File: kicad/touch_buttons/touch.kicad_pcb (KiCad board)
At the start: 2 copper layers, 15.7 x 15.7 mm, 3 parts, among them J1 CONN_01X03

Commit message: update
- drawing buttons
- still to finish
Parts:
- removed 2M1: R, Touch_conn:res
- removed J1: CONN_01X03, Touch_conn:touch_conn
- removed JP1: touch, Touch_conn:touch
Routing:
- net Net-(2M1-Pad2): track 36.9 -> 0.00 mm, vias 1 -> 0
- net Net-(2M1-Pad1): track 12.2 -> 0.00 mm
- net (no net): track 0.51 -> 0.00 mm, vias 1 -> 0
- removed copper zone on B.Cu, net GND
- removed copper zone on F.Cu, net GND
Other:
- board size 15.7 x 15.7 mm -> 15 x 15 mm

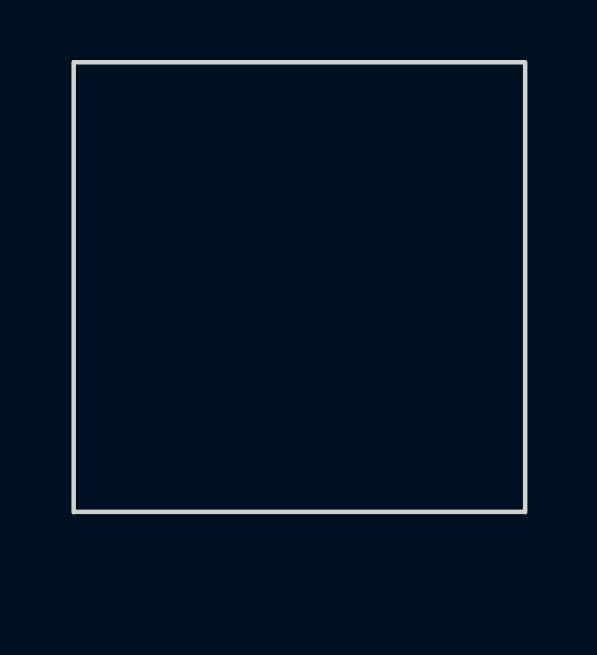
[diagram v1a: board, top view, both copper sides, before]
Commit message: update
- try to make a better button
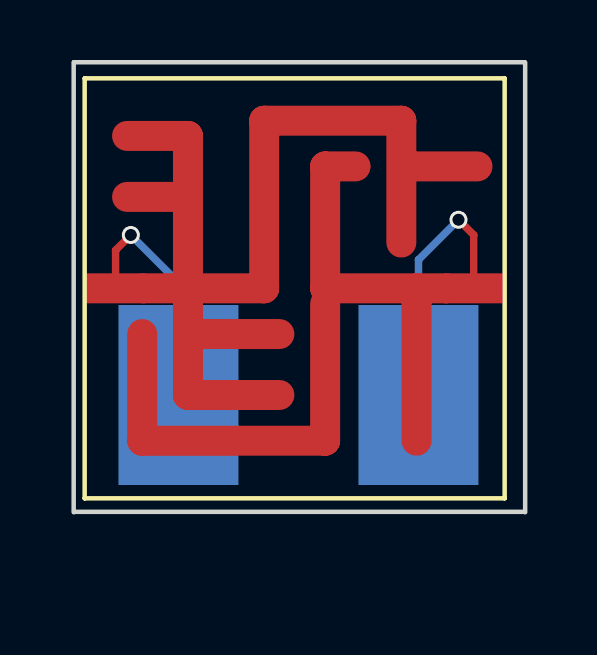
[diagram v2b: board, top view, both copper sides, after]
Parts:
- added J1: CONN_01X02, touch_conn, B.Cu at (157.5, 101.1)
- added JP1: touch, touch_zig, F.Cu at (157.4, 97.5)
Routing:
- net Net-(J1-Pad1): track 0.00 -> 8.89 mm, vias 0 -> 1
- net GND: track 0.00 -> 7.98 mm, vias 0 -> 1
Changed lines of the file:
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@@
-(kicad_pcb (version 4) (host pcbnew 4.0.6)
+(kicad_pcb (version 4) (host pcbnew 4.0.7)
   (general
-    (links 0)
+    (links 2)
     (no_connects 0)
-    (area 149.530999 91.110999 165.429001 107.009001)
+    (area 149.911999 89.924999 165.111501 105.075001)
     (thickness 1.6)
     (drawings 6)
-    (tracks 0)
+    (tracks 10)
     (zones 0)
-    (modules 0)
-    (nets 1)
+    (modules 2)
+    (nets 3)
   )
   (page A4)
@@
     (pad_drill 0)
     (pad_to_mask_clearance 0.2)
-    (aux_axis_origin 0 0)
+    (aux_axis_origin 188.468 96.3295)
     (visible_elements 7FFFFFFF)
     (pcbplotparams
@@
   )
   (net 0 "")
+  (net 1 "Net-(J1-Pad1)")
+  (net 2 GND)
   (net_class Default "This is the default net class."
     (clearance 0.2)
@@
     (uvia_dia 0.3)
     (uvia_drill 0.1)
+    (add_net GND)
+    (add_net "Net-(J1-Pad1)")
+  )
+  (module touch_zig (layer F.Cu)
+    (at 157.353 97.536)
+    (fp_text reference JP1 (at 0 9.652) (layer F.Fab)
+      (effects (font (size 1 1) (thickness 0.15)))
+    )
+    (fp_text value touch (at 0 8.128) (layer F.Fab)
+      (effects (font (size 1 1) (thickness 0.15)))
+    )
+    (fp_line (start 5.08 0) (end 1.016 0) (layer F.Cu) (width 1))
+    (fp_line (start -5.08 0) (end -1.016 0) (layer F.Cu) (width 1))
+    (fp_line (start 3.556 -5.588) (end 3.556 -1.524) (layer F.Cu) (width 1))
+    (fp_line (start -1.016 -5.588) (end 3.556 -5.588) (layer F.Cu) (width 1))
+    (fp_line (start -1.016 0) (end -1.016 -5.588) (layer F.Cu) (width 1))
+    (fp_line (start 1.016 -4.064) (end 2.032 -4.064) (layer F.Cu) (width 1))
+    (fp_line (start 1.016 0) (end 1.016 -4.064) (layer F.Cu) (width 1))
+    (fp_line (start -5.08 5.08) (end -5.08 1.524) (layer F.Cu) (width 1))
+    (fp_line (start 1.016 5.08) (end -5.08 5.08) (layer F.Cu) (width 1))
+    (fp_line (start 1.016 0.508) (end 1.016 5.08) (layer F.Cu) (width 1))
+    (fp_line (start -3.556 3.556) (end -0.508 3.556) (layer F.Cu) (width 1))
+    (fp_line (start -3.556 0.508) (end -3.556 3.556) (layer F.Cu) (width 1))
+    (fp_line (start -3.556 -5.08) (end -5.588 -5.08) (layer F.Cu) (width 1))
+    (fp_line (start -3.556 -0.508) (end -3.556 -5.08) (layer F.Cu) (width 1))
+    (fp_line (start 4.064 0) (end 4.064 5.08) (layer F.Cu) (width 1))
+    (fp_line (start 4.064 -4.064) (end 6.096 -4.064) (layer F.Cu) (width 1))
+    (fp_line (start -4.064 -3.048) (end -5.588 -3.048) (layer F.Cu) (width 1))
+    (fp_line (start -3.048 1.524) (end -0.508 1.524) (layer F.Cu) (width 1))
+    (fp_line (start -3.048 1.524) (end -0.508 1.524) (layer F.Mask) (width 1))
+    (fp_line (start -4.064 -3.048) (end -5.588 -3.048) (layer F.Mask) (width 1))
+    (fp_line (start 4.064 -4.064) (end 6.096 -4.064) (layer F.Mask) (width 1))
+    (fp_line (start 4.064 0) (end 4.064 5.08) (layer F.Mask) (width 1))
+    (fp_line (start -3.556 -0.508) (end -3.556 -5.08) (layer F.Mask) (width 1))
+    (fp_line (start -3.556 -5.08) (end -5.588 -5.08) (layer F.Mask) (width 1))
+    (fp_line (start -3.556 0.508) (end -3.556 3.556) (layer F.Mask) (width 1))
+    (fp_line (start -3.556 3.556) (end -0.508 3.556) (layer F.Mask) (width 1))
+    (fp_line (start 1.016 0.508) (end 1.016 5.08) (layer F.Mask) (width 1))
+    (fp_line (start 1.016 5.08) (end -5.08 5.08) (layer F.Mask) (width 1))
+    (fp_line (start -5.08 5.08) (end -5.08 1.524) (layer F.Mask) (width 1))
+    (fp_line (start 1.016 0) (end 1.016 -4.064) (layer F.Mask) (width 1))
+    (fp_line (start 1.016 -4.064) (end 2.032 -4.064) (layer F.Mask) (width 1))
+    (fp_line (start -1.016 0) (end -1.016 -5.588) (layer F.Mask) (width 1))
+    (fp_line (start -1.016 -5.588) (end 3.556 -5.588) (layer F.Mask) (width 1))
+    (fp_line (start 3.556 -5.588) (end 3.556 -1.524) (layer F.Mask) (width 1))
+    (fp_line (start -5.08 0) (end -1.016 0) (layer F.Mask) (width 1))
+    (fp_line (start 5.08 0) (end 1.016 0) (layer F.Mask) (width 1))
+    (fp_line (start -7 7) (end 7 7) (layer F.SilkS) (width 0.15))
+    (fp_line (start 7 7) (end 7 -7) (layer F.SilkS) (width 0.15))
+    (fp_line (start -7 -7) (end 7 -7) (layer F.SilkS) (width 0.15))
+    (fp_line (start -7 7) (end -7 -7) (layer F.SilkS) (width 0.15))
+    (pad 2 smd rect (at 5.969 0) (size 2 1) (layers F.Cu F.Paste F.Mask)
+      (net 1 "Net-(J1-Pad1)"))
+    (pad 1 smd rect (at -5.969 0) (size 2 1) (layers F.Cu F.Paste F.Mask)
+      (net 2 GND))
+  )
+  (module touch_conn (layer B.Cu)
+    (at 157.48 101.092 90)
+    (fp_text reference J1 (at 0 -7.112 90) (layer B.Fab)
+      (effects (font (size 1 1) (thickness 0.15)) (justify mirror))
+    )
+    (fp_text value CONN_01X02 (at 0 -8.89 90) (layer B.Fab)
+      (effects (font (size 1 1) (thickness 0.15)) (justify mirror))
+    )
+    (pad 2 smd rect (at 0 -4 90) (size 6 4) (layers B.Cu B.Paste B.Mask)
+      (net 2 GND))
+    (pad 1 smd rect (at 0 4 90) (size 6 4) (layers B.Cu B.Paste B.Mask)
+      (net 1 "Net-(J1-Pad1)"))
   )
   (dimension 14.986 (width 0.3) (layer Eco1.User)
@@
   (gr_line (start 149.987 90) (end 149.987 105) (angle 90) (layer Edge.Cuts) (width 0.15))
   (gr_line (start 150 90) (end 165 90) (angle 90) (layer Edge.Cuts) (width 0.15))
+  (segment (start 161.48 101.092) (end 161.48 96.584) (width 0.25) (layer B.Cu) (net 1))
+  (segment (start 163.322 95.758) (end 163.322 97.536) (width 0.25) (layer F.Cu) (net 1))
+  (segment (start 162.814 95.25) (end 163.322 95.758) (width 0.25) (layer F.Cu) (net 1))
+  (via (at 162.814 95.25) (size 0.6) (drill 0.4) (layers F.Cu B.Cu) (net 1))
+  (segment (start 161.48 96.584) (end 162.814 95.25) (width 0.25) (layer B.Cu) (net 1))
+  (segment (start 153.48 101.092) (end 153.48 97.346) (width 0.25) (layer B.Cu) (net 2))
+  (segment (start 151.384 96.266) (end 151.384 97.536) (width 0.25) (layer F.Cu) (net 2))
+  (segment (start 151.892 95.758) (end 151.384 96.266) (width 0.25) (layer F.Cu) (net 2))
+  (via (at 151.892 95.758) (size 0.6) (drill 0.4) (layers F.Cu B.Cu) (net 2))
+  (segment (start 153.48 97.346) (end 151.892 95.758) (width 0.25) (layer B.Cu) (net 2))
 )
